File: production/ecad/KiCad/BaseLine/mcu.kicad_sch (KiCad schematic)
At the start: 47 parts, among them J2 1332645, Q1 AO3400A, Q2 AO3400A, SW1 SW_Push, SW2 SW_Push, U2 ESP32-WROOM-32UE_M113EH6400UH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, U3 CP2102N-A02-GQFN28

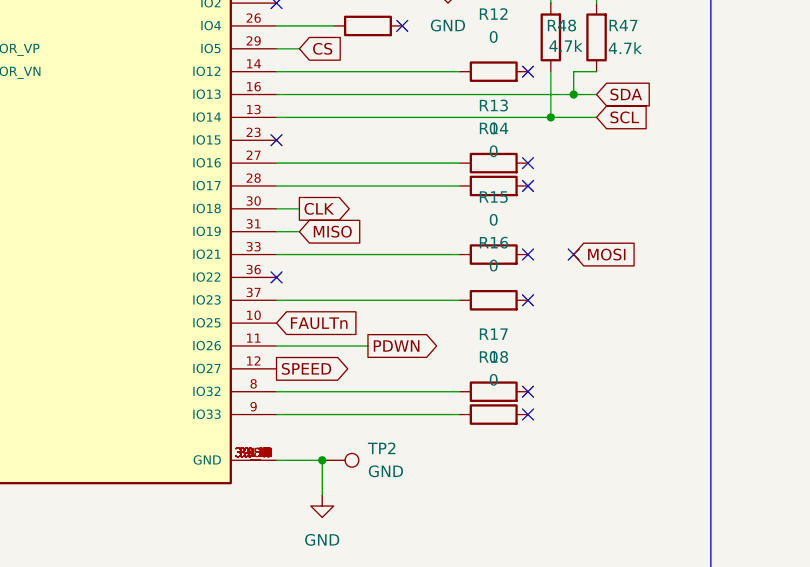
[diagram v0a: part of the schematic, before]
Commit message: Changed fault pin names
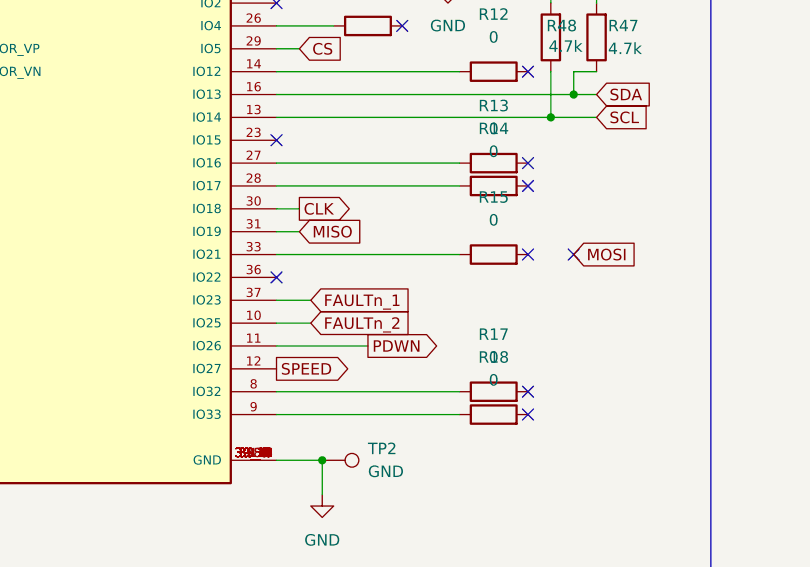
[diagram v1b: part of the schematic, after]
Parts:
- removed R16: 0, Resistor_SMD:R_0805_2012Metric, symbol Device:R
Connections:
- net FAULTn_1: now reaches U2.37 (IO23)
- net FAULTn renamed FAULTn_2
- no-connect marks 33 -> 32
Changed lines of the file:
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@@
 	)
 	(no_connect
-		(at 110.49 83.82)
-	)
-	(no_connect
 		(at 241.3 76.2)
 	)
@@
 	(wire
 		(pts
-			(xy 102.87 83.82) (xy 82.55 83.82)
-		)
-		(stroke
-			(width 0)
-			(type default)
-		)
-	)
-	(wire
-		(pts
 			(xy 110.49 185.42) (xy 110.49 186.69)
 		)
@@
 	(wire
 		(pts
+			(xy 86.36 83.82) (xy 82.55 83.82)
+		)
+		(stroke
+			(width 0)
+			(type default)
+		)
+	)
+	(wire
+		(pts
 			(xy 82.55 60.96) (xy 115.57 60.96)
 		)
@@
 	(wire
 		(pts
+			(xy 86.36 86.36) (xy 82.55 86.36)
+		)
+		(stroke
+			(width 0)
+			(type default)
+		)
+	)
+	(wire
+		(pts
 			(xy 259.08 50.8) (xy 269.24 50.8)
 		)
@@
 		)
 	)
-	(global_label "FAULTn"
+	(global_label "FAULTn_2"
 		(shape input)
-		(at 82.55 86.36 0)
+		(at 86.36 86.36 0)
 		(fields_autoplaced yes)
 		(effects
@@
 		)
 		(property "Intersheetrefs" "${INTERSHEET_REFS}"
-			(at 92.1876 86.36 0)
+			(at 98.1747 86.36 0)
 			(effects
 				(font
@@
 		)
 	)
+	(global_label "FAULTn_1"
+		(shape input)
+		(at 86.36 83.82 0)
+		(fields_autoplaced yes)
+		(effects
+			(font
+				(size 1.27 1.27)
+			)
+			(justify left)
+		)
+		(property "Intersheetrefs" "${INTERSHEET_REFS}"
+			(at 98.1747 83.82 0)
+			(effects
+				(font
+					(size 1.27 1.27)
+				)
+				(justify left)
+				(hide yes)
+			)
+		)
+	)
 	(global_label "UART_TXD"
 		(shape output)
@@
 					(unit 1)
 				)
-			)
-		)
-	)
-	(symbol
-		(lib_id "Device:R")
-		(at 106.68 83.82 90)
-		(unit 1)
-		(exclude_from_sim no)
-		(in_bom yes)
-		(on_board yes)
-		(dnp no)
-		(fields_autoplaced yes)
-		(property "Reference" "R16"
-			(at 106.68 77.47 90)
-			(effects
-				(font
-					(size 1.27 1.27)
-				)
-			)
-		)
-		(property "Value" "0"
-			(at 106.68 80.01 90)
-			(effects
-				(font
-					(size 1.27 1.27)
-				)
-			)
-		)
-		(property "Footprint" "Resistor_SMD:R_0805_2012Metric"
-			(at 106.68 85.598 90)
-			(effects
-				(font
-					(size 1.27 1.27)
-				)
-				(hide yes)
-			)
-		)
-		(property "Datasheet" "~"
-			(at 106.68 83.82 0)
-			(effects
-				(font
-					(size 1.27 1.27)
-				)
-				(hide yes)
-			)
-		)
-		(property "Description" "Resistor"
-			(at 106.68 83.82 0)
-			(effects
-				(font
-					(size 1.27 1.27)
-				)
-				(hide yes)
-			)
-		)
-		(pin "1"
-		)
-		(pin "2"
-		)
-		(instances
-			(project "BaseLine"
-				(path "/ba9eda21-3882-41e1-8265-3d8ac781da20/b5018713-9dac-4933-acc6-88fa6ef21dcb"
-					(reference "R16")
-					(unit 1)
-				)

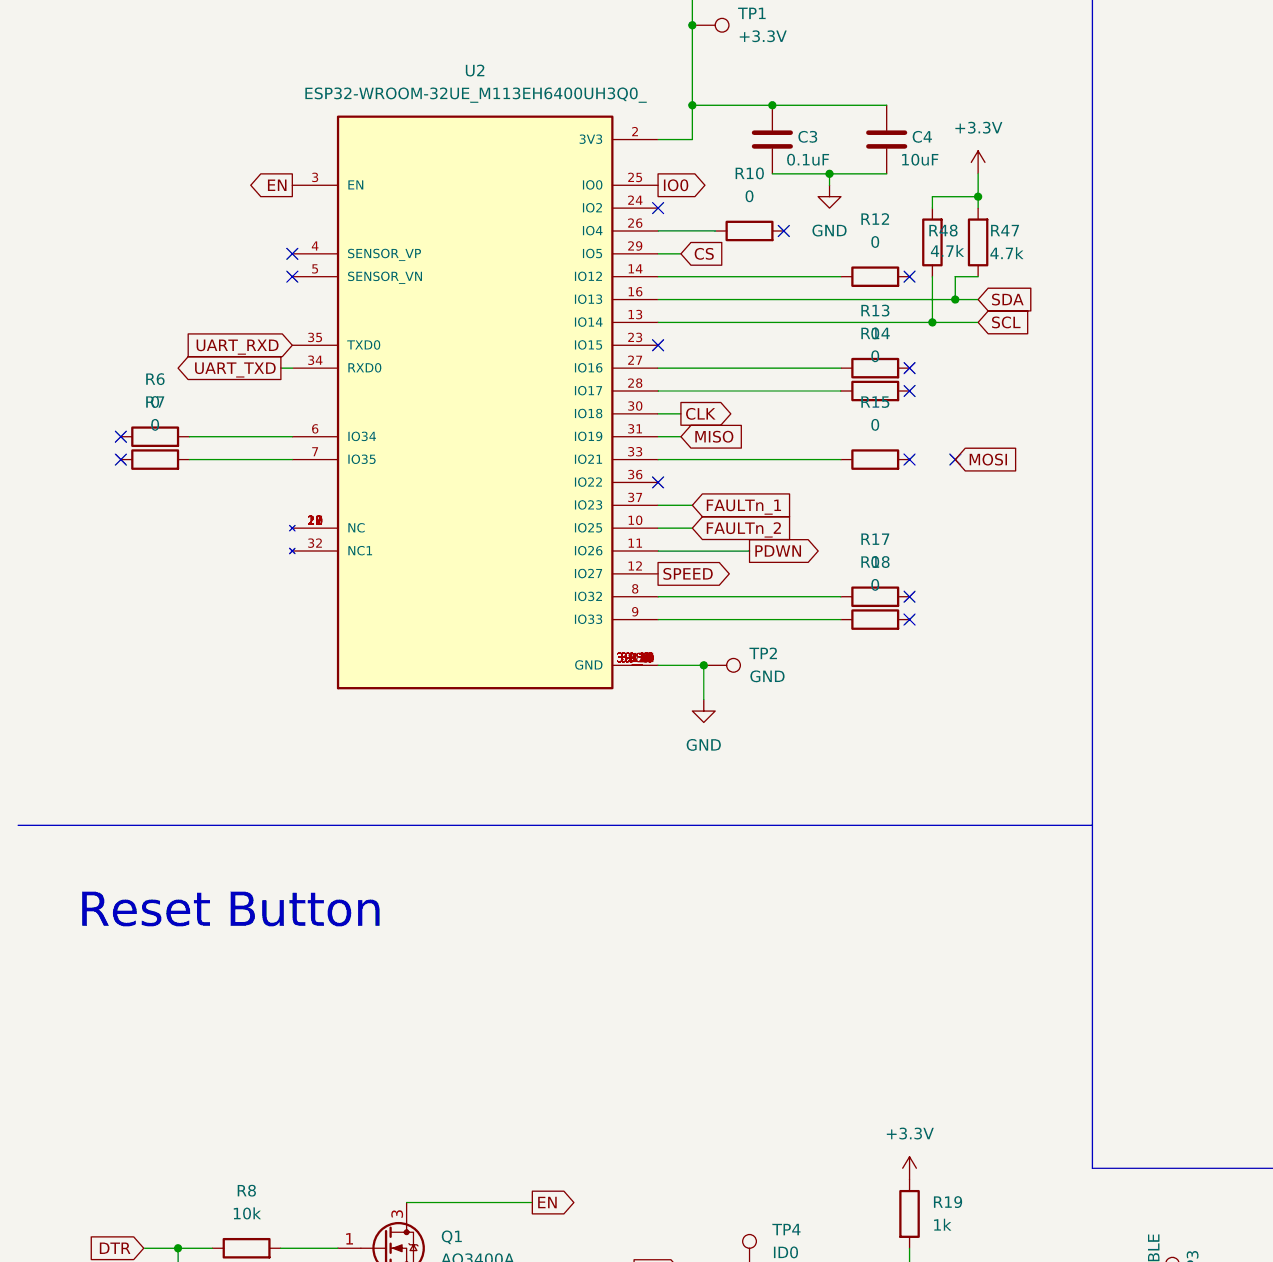
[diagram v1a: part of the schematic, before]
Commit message: Connectors and heirarchal labels
added connectors for power on the Loadcell schem and the battery schem

added the MCU heirarchal labels
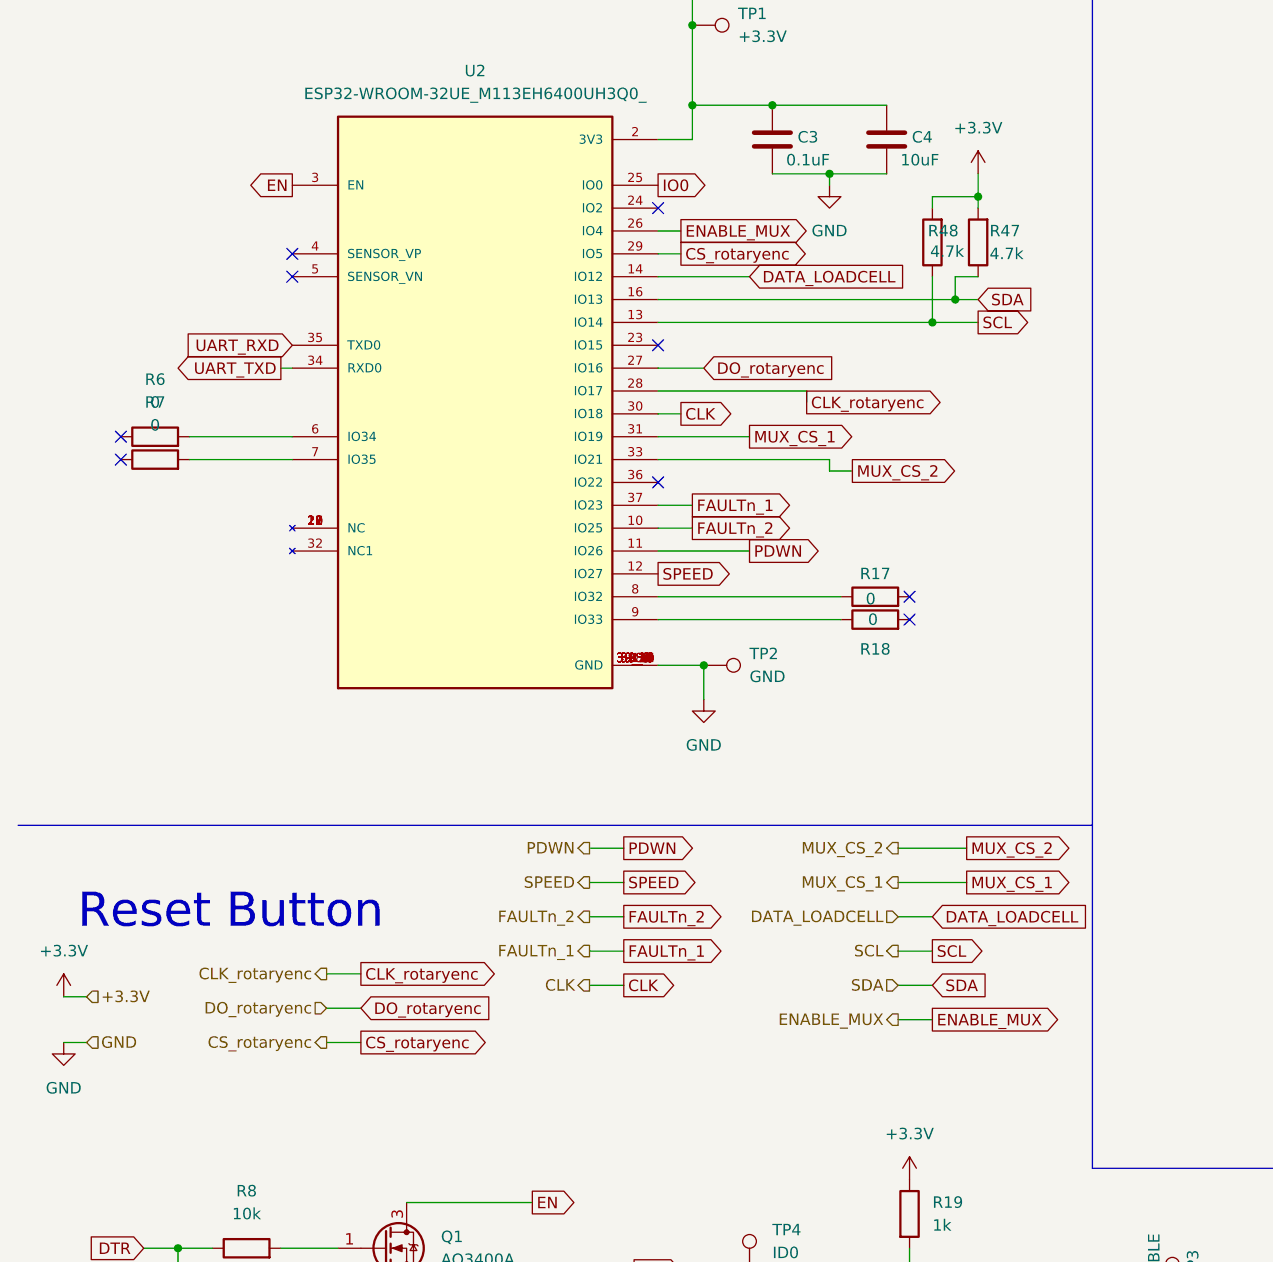
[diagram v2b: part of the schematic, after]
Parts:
- removed R10, R12, R13, R14, R15: 0, Resistor_SMD:R_0805_2012Metric, symbol Device:R
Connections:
- net CLK_rotaryenc: now reaches U2.28 (IO17)
- net ENABLE_MUX: now reaches U2.26 (IO4)
- net DATA_LOADCELL: now reaches U2.14 (IO12)
- net DO_rotaryenc: now reaches U2.27 (IO16)
- net MUX_CS_2: now reaches U2.33 (IO21)
- net CS renamed CS_rotaryenc
- net MISO renamed MUX_CS_1
- no-connect marks 32 -> 26

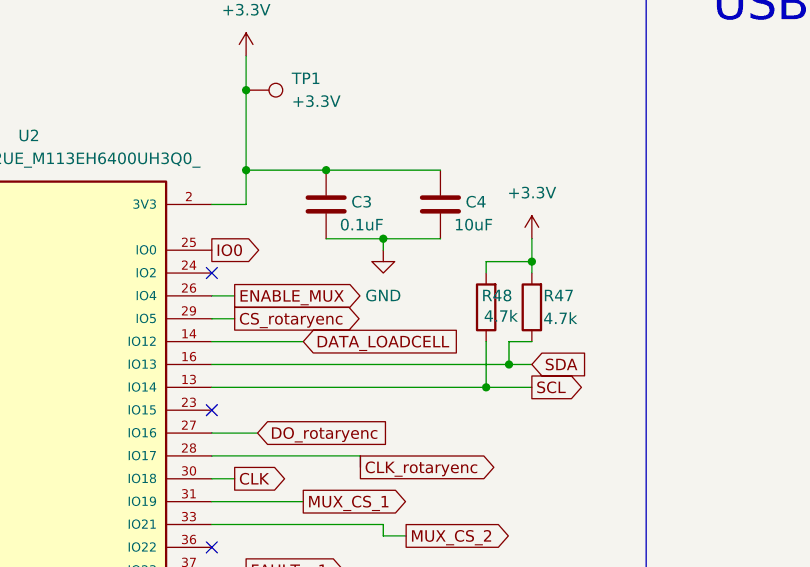
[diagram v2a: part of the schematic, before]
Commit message: fixing MUX
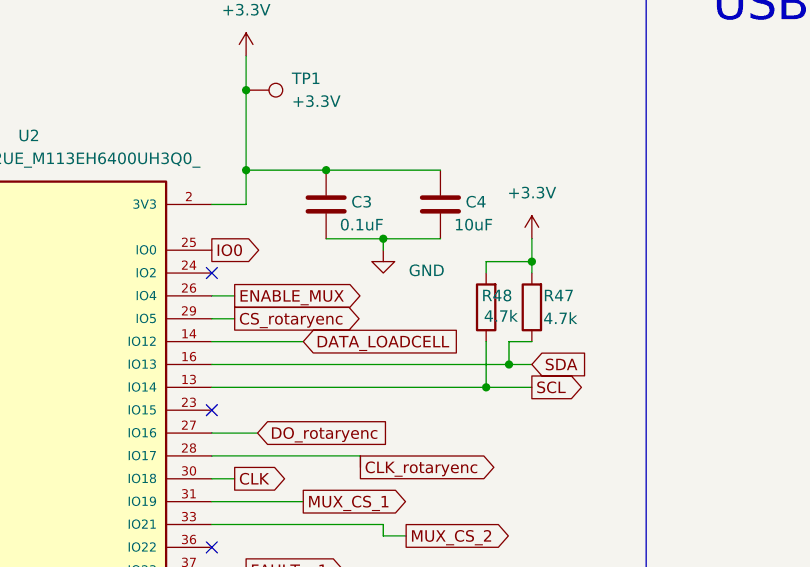
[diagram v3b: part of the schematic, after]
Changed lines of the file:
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@@
 		(on_board yes)
 		(dnp no)
-		(fields_autoplaced yes)
 		(property "Reference" "#PWR011"
 			(at 101.6 54.61 0)
@@
 		)
 		(property "Value" "GND"
-			(at 101.6 53.34 0)
+			(at 106.426 50.546 0)
 			(effects
 				(font

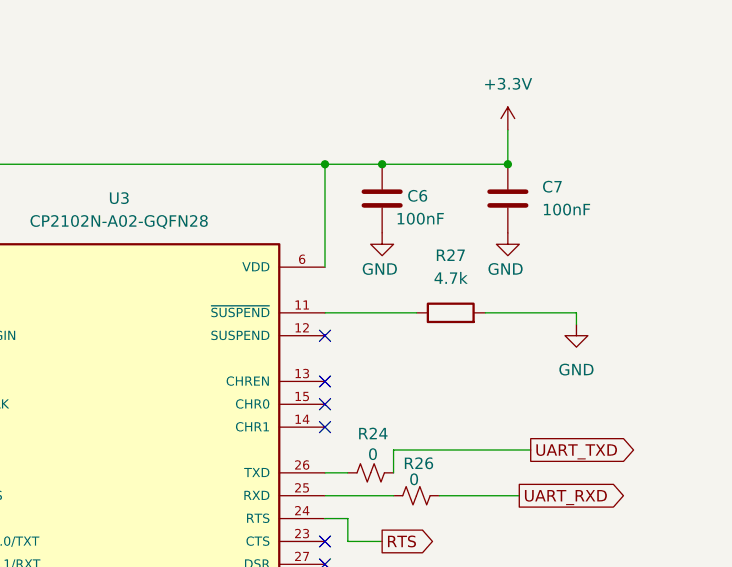
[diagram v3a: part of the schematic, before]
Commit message: fixed one resistor symbol
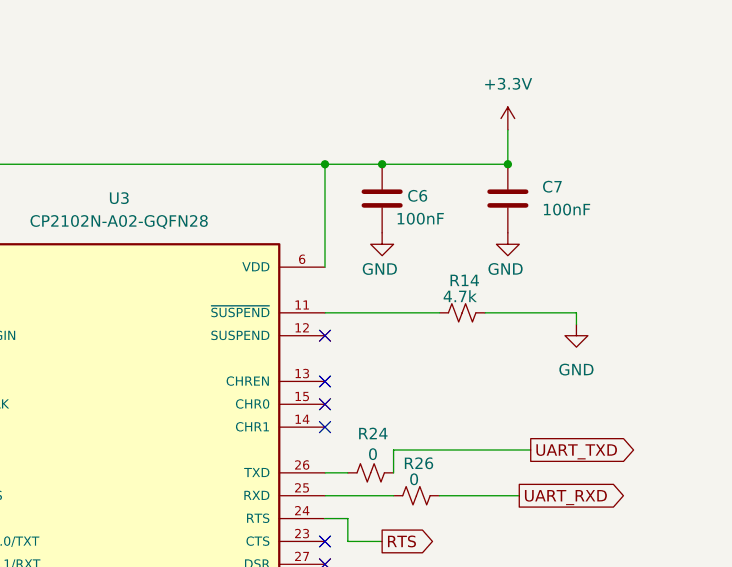
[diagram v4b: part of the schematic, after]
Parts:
- removed R27: 4.7k, Resistor_SMD:R_0805_2012Metric, symbol Device:R
- added R14: 4.7k, Resistor_SMD:R_0805_2012Metric, symbol Device:R_Small_US
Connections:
- net GND: now also R14.1
- net at U3.11 (~{SUSPEND}): now also R14.2
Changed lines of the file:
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@@
 	(wire
 		(pts
-			(xy 251.46 50.8) (xy 241.3 50.8)
+			(xy 241.3 50.8) (xy 254 50.8)
 		)
 		(stroke
@@
 	)
 	(symbol
-		(lib_id "Device:R")
-		(at 255.27 50.8 90)
-		(unit 1)
-		(exclude_from_sim no)
-		(in_bom yes)
-		(on_board yes)
-		(dnp no)
-		(fields_autoplaced yes)
-		(property "Reference" "R27"
-			(at 255.27 44.45 90)
-			(effects
-				(font
-					(size 1.27 1.27)
-				)
-			)
-		)
-		(property "Value" "4.7k"
-			(at 255.27 46.99 90)
-			(effects
-				(font
-					(size 1.27 1.27)
-				)
-			)
-		)
-		(property "Footprint" "Resistor_SMD:R_0805_2012Metric"
-			(at 255.27 52.578 90)
-			(effects
-				(font
-					(size 1.27 1.27)
-				)
-				(hide yes)
-			)
-		)
-		(property "Datasheet" "~"
-			(at 255.27 50.8 0)
-			(effects
-				(font
-					(size 1.27 1.27)
-				)
-				(hide yes)
-			)
-		)
-		(property "Description" "Resistor"
-			(at 255.27 50.8 0)
-			(effects
-				(font
-					(size 1.27 1.27)
-				)
-				(hide yes)
-			)
-		)
-		(pin "1"
-		)
-		(pin "2"
-		)
-		(instances
-			(project "BaseLine"
-				(path "/ba9eda21-3882-41e1-8265-3d8ac781da20/b5018713-9dac-4933-acc6-88fa6ef21dcb"
-					(reference "R27")
-					(unit 1)
-				)
-			)
-		)
-	)
-	(symbol
 		(lib_id "power:+3.3V")
 		(at 261.62 30.48 0)
@@
 					(unit 1)
 				)
+			)
+		)
+	)
+	(symbol
+		(lib_id "Device:R_Small_US")
+		(at 256.54 50.8 270)
+		(unit 1)
+		(exclude_from_sim no)
+		(in_bom yes)
+		(on_board yes)
+		(dnp no)
+		(property "Reference" "R14"
+			(at 256.794 47.244 90)
+			(effects
+				(font
+					(size 1.27 1.27)
+				)
+			)
+		)
+		(property "Value" "4.7k"
+			(at 256.286 49.022 90)
+			(effects
+				(font
+					(size 1.27 1.27)
+				)
+			)
+		)
+		(property "Footprint" "Resistor_SMD:R_0805_2012Metric"
+			(at 256.54 50.8 0)
+			(effects
+				(font
+					(size 1.27 1.27)
+				)
+				(hide yes)
+			)
+		)
+		(property "Datasheet" "~"
+			(at 256.54 50.8 0)
+			(effects
+				(font
+					(size 1.27 1.27)
+				)
+				(hide yes)
+			)
+		)
+		(property "Description" "Resistor, small US symbol"
+			(at 256.54 50.8 0)
+			(effects
+				(font
+					(size 1.27 1.27)
+				)
+				(hide yes)
+			)
+		)
+		(pin "1"
+		)
+		(pin "2"
+		)
+		(instances
+			(project "BaseLine"
+				(path "/ba9eda21-3882-41e1-8265-3d8ac781da20/b5018713-9dac-4933-acc6-88fa6ef21dcb"
+					(reference "R14")
+					(unit 1)
+				)

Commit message: Added some footprints
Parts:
- R22: footprint (none) -> Resistor_SMD:R_0805_2012Metric_Pad1.20x1.40mm_HandSolder
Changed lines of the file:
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@@
 			)
 		)
-		(property "Footprint" ""
+		(property "Footprint" "Resistor_SMD:R_0805_2012Metric_Pad1.20x1.40mm_HandSolder"
 			(at 181.61 127 0)
 			(effects

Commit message: Test point footprints changed
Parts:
- TP1, TP2, TP3, TP4, TP5, TP6, TP7: footprint (none) -> TestPoint:TestPoint_Pad_2.0x2.0mm
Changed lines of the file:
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@@
 			)
 		)
-		(property "Footprint" ""
+		(property "Footprint" "TestPoint:TestPoint_Pad_2.0x2.0mm"
 			(at 97.79 168.91 0)
 			(effects
@@
 			)
 		)
-		(property "Footprint" ""
+		(property "Footprint" "TestPoint:TestPoint_Pad_2.0x2.0mm"
 			(at 190.5 43.18 0)
 			(effects
@@
 			)
 		)
-		(property "Footprint" ""
+		(property "Footprint" "TestPoint:TestPoint_Pad_2.0x2.0mm"
 			(at 86.36 35.56 0)
 			(effects
@@
 			)
 		)
-		(property "Footprint" ""
+		(property "Footprint" "TestPoint:TestPoint_Pad_2.0x2.0mm"
 			(at 87.63 106.68 0)
 			(effects
@@
 			)
 		)
-		(property "Footprint" ""
+		(property "Footprint" "TestPoint:TestPoint_Pad_2.0x2.0mm"
 			(at 252.73 99.06 0)
 			(effects
@@
 			)
 		)
-		(property "Footprint" ""
+		(property "Footprint" "TestPoint:TestPoint_Pad_2.0x2.0mm"
 			(at 181.61 40.64 0)
 			(effects
@@
 			)
 		)
-		(property "Footprint" ""
+		(property "Footprint" "TestPoint:TestPoint_Pad_2.0x2.0mm"
 			(at 144.78 171.45 0)
 			(effects

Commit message: added cp2102 footprint
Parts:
- SW1, SW2: footprint CSTAR-MainBoard-Footprints:SW_1825910-6-4 -> 1825910_6:SW_1825910-6-4
- U3: footprint CP2102N-A02-GQFN28:QFN50P500X500X80-29N -> CP2102N_A02_GQFN28:QFN50P500X500X80-29N
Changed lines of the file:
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@@
 			)
 		)
-		(property "Footprint" "CSTAR-MainBoard-Footprints:SW_1825910-6-4"
+		(property "Footprint" "1825910_6:SW_1825910-6-4"
 			(at 161.29 181.61 0)
 			(effects
@@
 			)
 		)
-		(property "Footprint" "CP2102N-A02-GQFN28:QFN50P500X500X80-29N"
+		(property "Footprint" "CP2102N_A02_GQFN28:QFN50P500X500X80-29N"
 			(at 218.44 73.66 0)
 			(effects
@@
 			)
 		)
-		(property "Footprint" "CSTAR-MainBoard-Footprints:SW_1825910-6-4"
+		(property "Footprint" "1825910_6:SW_1825910-6-4"
 			(at 115.57 177.8 0)
 			(effects
